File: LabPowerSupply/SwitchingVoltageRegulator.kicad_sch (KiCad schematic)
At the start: 14 parts

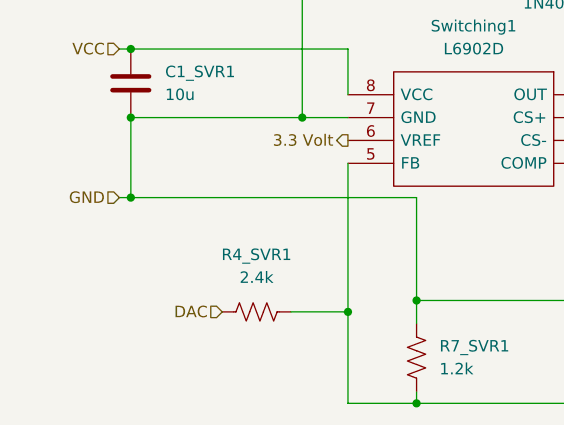
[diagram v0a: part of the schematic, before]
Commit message: Fixed oscillator caps, began changing resistors to more common values
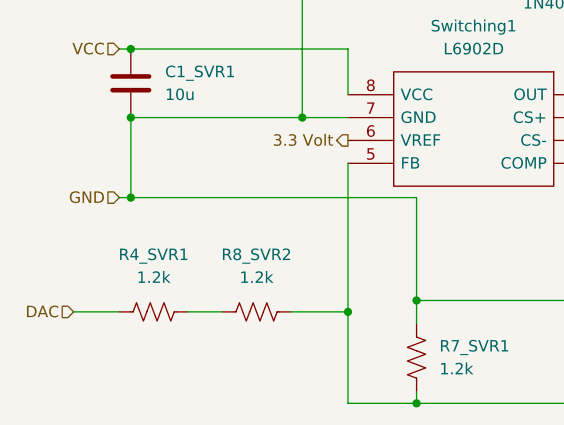
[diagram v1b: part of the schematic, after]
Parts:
- added R8_SVR2: 1.2k, Resistor_SMD:R_0603_1608Metric, symbol Device:R_US
- R4_SVR1: value 2.4k -> 1.2k
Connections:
- net FeedBack: now also R8_SVR2.1; no longer R4_SVR1.1
- new net: R4_SVR1.1, R8_SVR2.2
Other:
- moved on the sheet: R4_SVR1
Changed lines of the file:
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@@
   (junction (at 86.36 87.63) (diameter 0) (color 0 0 0 0)
   )
+  (junction (at 138.43 115.57) (diameter 0) (color 0 0 0 0)
+  )
+  (junction (at 151.13 92.71) (diameter 0) (color 0 0 0 0)
+  )
+  (junction (at 158.75 115.57) (diameter 0) (color 0 0 0 0)
+  )
+  (junction (at 138.43 100.33) (diameter 0) (color 0 0 0 0)
+  )
+  (junction (at 86.36 104.14) (diameter 0) (color 0 0 0 0)
+  )
+  (junction (at 166.37 97.79) (diameter 0) (color 0 0 0 0)
+  )
   (junction (at 110.49 116.84) (diameter 0) (color 0 0 0 0)
   )
-  (junction (at 138.43 115.57) (diameter 0) (color 0 0 0 0)
-  )
-  (junction (at 151.13 92.71) (diameter 0) (color 0 0 0 0)
-  )
-  (junction (at 158.75 115.57) (diameter 0) (color 0 0 0 0)
-  )
-  (junction (at 138.43 100.33) (diameter 0) (color 0 0 0 0)
-  )
-  (junction (at 86.36 104.14) (diameter 0) (color 0 0 0 0)
-  )
-  (junction (at 166.37 97.79) (diameter 0) (color 0 0 0 0)
-  )
   (junction (at 166.37 92.71) (diameter 0) (color 0 0 0 0)
   )
@@
     (stroke (width 0) (type default) (color 0 0 0 0))
   )
+  (wire (pts (xy 118.11 115.57) (xy 138.43 115.57))
+    (stroke (width 0) (type default) (color 0 0 0 0))
+  )
+  (wire (pts (xy 158.75 100.33) (xy 138.43 100.33))
+    (stroke (width 0) (type default) (color 0 0 0 0))
+  )
+  (wire (pts (xy 151.13 92.71) (xy 151.13 95.25))
+    (stroke (width 0) (type default) (color 0 0 0 0))
+  )
+  (wire (pts (xy 166.37 92.71) (xy 171.45 92.71))
+    (stroke (width 0) (type default) (color 0 0 0 0))
+  )
   (wire (pts (xy 110.49 116.84) (xy 110.49 127))
     (stroke (width 0) (type default) (color 0 0 0 0))
   )
-  (wire (pts (xy 118.11 115.57) (xy 138.43 115.57))
-    (stroke (width 0) (type default) (color 0 0 0 0))
-  )
-  (wire (pts (xy 158.75 100.33) (xy 138.43 100.33))
-    (stroke (width 0) (type default) (color 0 0 0 0))
-  )
-  (wire (pts (xy 151.13 92.71) (xy 151.13 95.25))
-    (stroke (width 0) (type default) (color 0 0 0 0))
-  )
-  (wire (pts (xy 166.37 92.71) (xy 171.45 92.71))
-    (stroke (width 0) (type default) (color 0 0 0 0))
-  )
   (wire (pts (xy 85.09 87.63) (xy 86.36 87.63))
     (stroke (width 0) (type default) (color 0 0 0 0))
@@
     (stroke (width 0) (type default) (color 0 0 0 0))
   )
+  (wire (pts (xy 92.71 116.84) (xy 96.52 116.84))
+    (stroke (width 0) (type default) (color 0 0 0 0))
+  )
   (wire (pts (xy 157.48 92.71) (xy 151.13 92.71))
     (stroke (width 0) (type default) (color 0 0 0 0))
   )
+  (wire (pts (xy 80.01 116.84) (xy 85.09 116.84))
+    (stroke (width 0) (type default) (color 0 0 0 0))
+  )
   (wire (pts (xy 105.41 76.2) (xy 140.97 76.2))
     (stroke (width 0) (type default) (color 0 0 0 0))
@@
     (stroke (width 0) (type default) (color 0 0 0 0))
   )
+  (wire (pts (xy 104.14 116.84) (xy 110.49 116.84))
+    (stroke (width 0) (type default) (color 0 0 0 0))
+  )
   (wire (pts (xy 140.97 77.47) (xy 140.97 76.2))
     (stroke (width 0) (type default) (color 0 0 0 0))
@@
   )
   (wire (pts (xy 171.45 85.09) (xy 171.45 92.71))
-    (stroke (width 0) (type default) (color 0 0 0 0))
-  )
-  (wire (pts (xy 104.14 116.84) (xy 110.49 116.84))
     (stroke (width 0) (type default) (color 0 0 0 0))
   )
@@
     (effects (font (size 1.27 1.27)) (justify left bottom))
   )
-  (hierarchical_label "DAC" (shape input) (at 96.52 116.84 180)
+  (hierarchical_label "DAC" (shape input) (at 80.01 116.84 180)
     (effects (font (size 1.27 1.27)) (justify right))
   )
@@
     (pin "2")
   )
+  (symbol (lib_id "Device:R_US") (at 88.9 116.84 270) (unit 1)
+    (in_bom yes) (on_board yes) (fields_autoplaced)
+    (property "Reference" "R4_SVR1" (id 0) (at 88.9 110.49 90))
+    (property "Value" "1.2k" (id 1) (at 88.9 113.03 90))
+    (property "Footprint" "Resistor_SMD:R_0603_1608Metric" (id 2) (at 88.646 117.856 90)
+      (effects (font (size 1.27 1.27)) hide)
+    )
+    (property "Datasheet" "~" (id 3) (at 88.9 116.84 0)
+      (effects (font (size 1.27 1.27)) hide)
+    )
+    (pin "1")
+    (pin "2")
+  )
+  (symbol (lib_id "Device:R_US") (at 184.15 110.49 0) (unit 1)
+    (in_bom yes) (on_board yes) (fields_autoplaced)
+    (property "Reference" "R6_SVR1" (id 0) (at 186.69 109.2199 0)
+      (effects (font (size 1.27 1.27)) (justify left))
+    )
+    (property "Value" "1k" (id 1) (at 186.69 111.7599 0)
+      (effects (font (size 1.27 1.27)) (justify left))
+    )
+    (property "Footprint" "Resistor_SMD:R_0603_1608Metric" (id 2) (at 185.166 110.744 90)
+      (effects (font (size 1.27 1.27)) hide)
+    )
+    (property "Datasheet" "~" (id 3) (at 184.15 110.49 0)
+      (effects (font (size 1.27 1.27)) hide)
+    )
+    (pin "1")
+    (pin "2")
+  )
   (symbol (lib_id "Device:R_US") (at 100.33 116.84 270) (unit 1)
     (in_bom yes) (on_board yes) (fields_autoplaced)
-    (property "Reference" "R4_SVR1" (id 0) (at 100.33 110.49 90))
-    (property "Value" "2.4k" (id 1) (at 100.33 113.03 90))
+    (property "Reference" "R8_SVR2" (id 0) (at 100.33 110.49 90))
+    (property "Value" "1.2k" (id 1) (at 100.33 113.03 90))
     (property "Footprint" "Resistor_SMD:R_0603_1608Metric" (id 2) (at 100.076 117.856 90)
       (effects (font (size 1.27 1.27)) hide)
@@
       (effects (font (size 1.27 1.27)) hide)
     )
-    (pin "1")
-    (pin "2")
-  )
-  (symbol (lib_id "Device:R_US") (at 184.15 110.49 0) (unit 1)
-    (in_bom yes) (on_board yes) (fields_autoplaced)
-    (property "Reference" "R6_SVR1" (id 0) (at 186.69 109.2199 0)
-      (effects (font (size 1.27 1.27)) (justify left))
-    )
-    (property "Value" "1k" (id 1) (at 186.69 111.7599 0)
-      (effects (font (size 1.27 1.27)) (justify left))
-    )
-    (property "Footprint" "Resistor_SMD:R_0603_1608Metric" (id 2) (at 185.166 110.744 90)
-      (effects (font (size 1.27 1.27)) hide)
-    )
-    (property "Datasheet" "~" (id 3) (at 184.15 110.49 0)
-      (effects (font (size 1.27 1.27)) hide)
-    )

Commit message: in the middle
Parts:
- renumbered R8_SVR2 to R8_SVR1
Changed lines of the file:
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@@
   (symbol (lib_id "Device:R_US") (at 100.33 116.84 270) (unit 1)
     (in_bom yes) (on_board yes) (fields_autoplaced)
-    (property "Reference" "R8_SVR2" (id 0) (at 100.33 110.49 90))
+    (property "Reference" "R8_SVR1" (id 0) (at 100.33 110.49 90))
     (property "Value" "1.2k" (id 1) (at 100.33 113.03 90))
     (property "Footprint" "Resistor_SMD:R_0603_1608Metric" (id 2) (at 100.076 117.856 90)

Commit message: Start tallying
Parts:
- L_SVR1: footprint Inductor_THT:L_Radial_D6.0mm_P4.00mm -> Inductor_SMD:L_Sumida_CR75
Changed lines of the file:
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@@
     (property "Reference" "L_SVR1" (id 0) (at 147.32 86.36 90))
     (property "Value" "22u" (id 1) (at 147.32 88.9 90))
-    (property "Footprint" "Inductor_THT:L_Radial_D6.0mm_P4.00mm" (id 2) (at 147.32 92.71 0)
+    (property "Footprint" "Inductor_SMD:L_Sumida_CR75" (id 2) (at 147.32 92.71 0)
       (effects (font (size 1.27 1.27)) hide)
     )

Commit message: almost done
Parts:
- removed R3_SVR1: 4k, Resistor_SMD:R_0603_1608Metric, symbol Device:R_US
- added R31_SVR1, R32_SVR1: 2k, Resistor_SMD:R_0603_1608Metric, symbol Device:R_US
- C3_SVR1, C4_SVR1: footprint Capacitor_SMD:C_0805_2012Metric -> Capacitor_SMD:C_0603_1608Metric
- renumbered R4_SVR1 to R41_SVR1, R8_SVR1 to R42_SVR1
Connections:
- net ADC: now also R32_SVR1.2
- net Switching Output: now also R31_SVR1.1
- new net: R31_SVR1.2, R32_SVR1.1
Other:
- moved on the sheet: R6_SVR1, R7_SVR1

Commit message: Changed capacitors to x7r
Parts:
- C1_SVR1: footprint Capacitor_SMD:C_0805_2012Metric -> Capacitor_SMD:C_1210_3225Metric
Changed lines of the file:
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@@
       (effects (font (size 1.27 1.27)) (justify left))
     )
-    (property "Footprint" "Capacitor_SMD:C_0805_2012Metric" (id 2) (at 87.3252 95.25 0)
+    (property "Footprint" "Capacitor_SMD:C_1210_3225Metric" (id 2) (at 87.3252 95.25 0)
       (effects (font (size 1.27 1.27)) hide)
     )

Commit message: Fixed cap footprints
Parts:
- C1_SVR1: footprint Capacitor_SMD:C_1210_3225Metric -> Capacitor_SMD:C_1206_3216Metric
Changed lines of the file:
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@@
       (effects (font (size 1.27 1.27)) (justify left))
     )
-    (property "Footprint" "Capacitor_SMD:C_1210_3225Metric" (id 2) (at 87.3252 95.25 0)
+    (property "Footprint" "Capacitor_SMD:C_1206_3216Metric" (id 2) (at 87.3252 95.25 0)
       (effects (font (size 1.27 1.27)) hide)
     )

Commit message: Changed grid size, began regrouping
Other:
- moved on the sheet: R41_SVR1, R42_SVR1
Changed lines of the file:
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@@
   (junction (at 166.37 97.79) (diameter 0) (color 0 0 0 0)
   )
-  (junction (at 110.49 116.84) (diameter 0) (color 0 0 0 0)
-  )
   (junction (at 166.37 92.71) (diameter 0) (color 0 0 0 0)
   )
@@
     (stroke (width 0) (type default) (color 0 0 0 0))
   )
+  (wire (pts (xy 100.33 134.62) (xy 118.11 134.62))
+    (stroke (width 0) (type default) (color 0 0 0 0))
+  )
   (wire (pts (xy 143.51 92.71) (xy 140.97 92.71))
     (stroke (width 0) (type default) (color 0 0 0 0))
@@
     (stroke (width 0) (type default) (color 0 0 0 0))
   )
-  (wire (pts (xy 110.49 116.84) (xy 110.49 127))
+  (wire (pts (xy 110.49 100.33) (xy 110.49 127))
     (stroke (width 0) (type default) (color 0 0 0 0))
   )
@@
     (stroke (width 0) (type default) (color 0 0 0 0))
   )
-  (wire (pts (xy 110.49 100.33) (xy 110.49 116.84))
-    (stroke (width 0) (type default) (color 0 0 0 0))
-  )
   (wire (pts (xy 180.34 105.41) (xy 166.37 105.41))
     (stroke (width 0) (type default) (color 0 0 0 0))
@@
     (stroke (width 0) (type default) (color 0 0 0 0))
   )
-  (wire (pts (xy 92.71 116.84) (xy 96.52 116.84))
+  (wire (pts (xy 88.9 134.62) (xy 92.71 134.62))
     (stroke (width 0) (type default) (color 0 0 0 0))
   )
@@
     (stroke (width 0) (type default) (color 0 0 0 0))
   )
-  (wire (pts (xy 80.01 116.84) (xy 85.09 116.84))
+  (wire (pts (xy 76.2 134.62) (xy 81.28 134.62))
     (stroke (width 0) (type default) (color 0 0 0 0))
   )
@@
     (stroke (width 0) (type default) (color 0 0 0 0))
   )
-  (wire (pts (xy 104.14 116.84) (xy 110.49 116.84))
-    (stroke (width 0) (type default) (color 0 0 0 0))
-  )
   (wire (pts (xy 140.97 77.47) (xy 140.97 76.2))
     (stroke (width 0) (type default) (color 0 0 0 0))
@@
   )
   (wire (pts (xy 180.34 105.41) (xy 180.34 127))
+    (stroke (width 0) (type default) (color 0 0 0 0))
+  )
+  (wire (pts (xy 118.11 127) (xy 118.11 134.62))
     (stroke (width 0) (type default) (color 0 0 0 0))
   )
@@
     (effects (font (size 1.27 1.27)) (justify left bottom))
   )
-  (hierarchical_label "DAC" (shape input) (at 80.01 116.84 180)
+  (hierarchical_label "DAC" (shape input) (at 76.2 134.62 180)
     (effects (font (size 1.27 1.27)) (justify right))
   )
@@
     (pin "2")
   )
-  (symbol (lib_id "Device:R_US") (at 88.9 116.84 270) (unit 1)
-    (in_bom yes) (on_board yes) (fields_autoplaced)
-    (property "Reference" "R41_SVR1" (id 0) (at 88.9 110.49 90))
-    (property "Value" "1.2k" (id 1) (at 88.9 113.03 90))
-    (property "Footprint" "Resistor_SMD:R_0603_1608Metric" (id 2) (at 88.646 117.856 90)
-      (effects (font (size 1.27 1.27)) hide)
-    )
-    (property "Datasheet" "~" (id 3) (at 88.9 116.84 0)
+  (symbol (lib_id "Device:R_US") (at 85.09 134.62 270) (unit 1)
+    (in_bom yes) (on_board yes) (fields_autoplaced)
+    (property "Reference" "R41_SVR1" (id 0) (at 85.09 128.27 90))
+    (property "Value" "1.2k" (id 1) (at 85.09 130.81 90))
+    (property "Footprint" "Resistor_SMD:R_0603_1608Metric" (id 2) (at 84.836 135.636 90)
+      (effects (font (size 1.27 1.27)) hide)
+    )
+    (property "Datasheet" "~" (id 3) (at 85.09 134.62 0)
       (effects (font (size 1.27 1.27)) hide)
     )
@@
     (pin "2")
   )
-  (symbol (lib_id "Device:R_US") (at 100.33 116.84 270) (unit 1)
-    (in_bom yes) (on_board yes) (fields_autoplaced)
-    (property "Reference" "R42_SVR1" (id 0) (at 100.33 110.49 90))
-    (property "Value" "1.2k" (id 1) (at 100.33 113.03 90))
-    (property "Footprint" "Resistor_SMD:R_0603_1608Metric" (id 2) (at 100.076 117.856 90)
-      (effects (font (size 1.27 1.27)) hide)
-    )
-    (property "Datasheet" "~" (id 3) (at 100.33 116.84 0)
-      (effects (font (size 1.27 1.27)) hide)
-    )
+  (symbol (lib_id "Device:R_US") (at 96.52 134.62 270) (unit 1)
+    (in_bom yes) (on_board yes) (fields_autoplaced)
+    (property "Reference" "R42_SVR1" (id 0) (at 96.52 128.27 90))
+    (property "Value" "1.2k" (id 1) (at 96.52 130.81 90))
+    (property "Footprint" "Resistor_SMD:R_0603_1608Metric" (id 2) (at 96.266 135.636 90)
+      (effects (font (size 1.27 1.27)) hide)
+    )
+    (property "Datasheet" "~" (id 3) (at 96.52 134.62 0)
+      (effects (font (size 1.27 1.27)) hide)
+    )

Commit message: Began routing modules
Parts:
- Switching1: footprint Package_SO:SOIC-8-1EP_3.9x4.9mm_P1.27mm_EP2.95x4.9mm_Mask2.71x3.4mm -> Package_SO:SO-8_3.9x4.9mm_P1.27mm
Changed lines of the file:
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@@
     (property "Reference" "Switching1" (id 0) (at 124.46 85.09 0))
     (property "Value" "L6902D" (id 1) (at 124.46 87.63 0))
-    (property "Footprint" "Package_SO:SOIC-8-1EP_3.9x4.9mm_P1.27mm_EP2.95x4.9mm_Mask2.71x3.4mm" (id 2) (at 114.3 90.17 0)
+    (property "Footprint" "Package_SO:SO-8_3.9x4.9mm_P1.27mm" (id 2) (at 114.3 90.17 0)
       (effects (font (size 1.27 1.27)) (justify left) hide)
     )
